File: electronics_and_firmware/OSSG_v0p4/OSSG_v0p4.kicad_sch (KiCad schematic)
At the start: 42 parts, among them J1 Conn_01x05_Male, Q1 2SC4617R BR, Q2 2SC4617R BR, SW1 SW_SPST, U1 SPH0645LMH, U2 ESP32-PICO-D4, U3 CH9102F

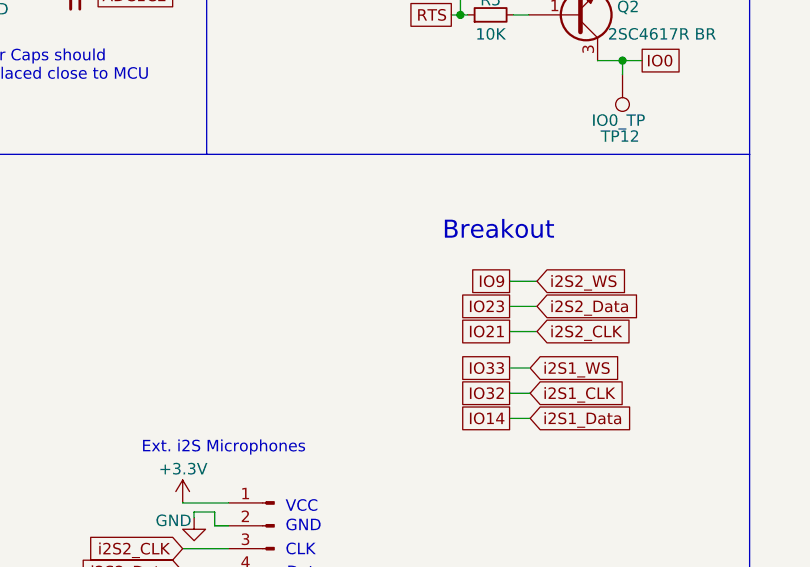
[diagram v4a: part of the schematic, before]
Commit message: adding in last update for the 2S branch design
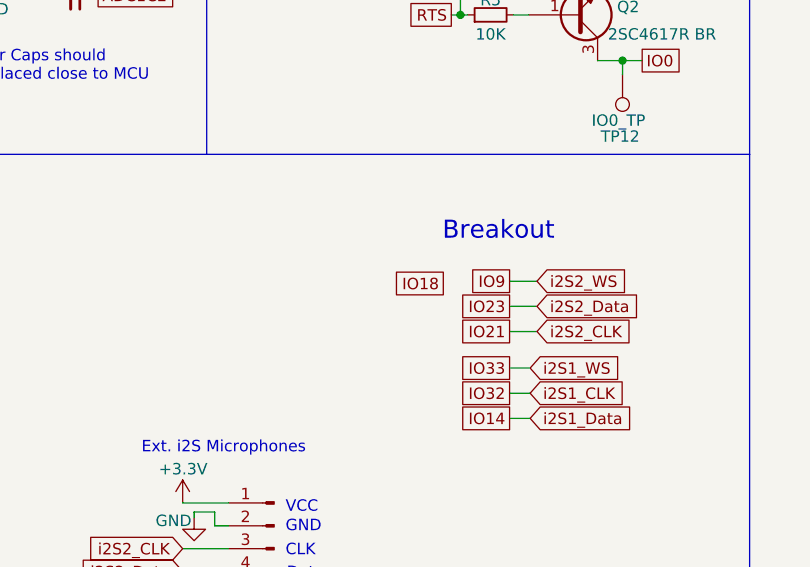
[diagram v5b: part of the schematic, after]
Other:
- title: Open Source Smart Glasses v0.4 -> Team OpenSource Smartglasses
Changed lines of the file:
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@@
   (paper "A3")
   (title_block
-    (title "Open Source Smart Glasses v0.4")
-    (date "2022-09-14")
-    (rev "0.4")
+    (title "Team OpenSource Smartglasses")
+    (date "2022-09-15")
+    (rev "V0.4b1")
     (company "Team Open Smart Glasses")
     (comment 1 "Design: Cayden Pierce, Nicholas Gray, Paul Hamilton")
@@
     (effects (font (size 1.27 1.27)) (justify right))
     (property "Intersheet References" "${INTERSHEET_REFS}" (id 0) (at 21.1726 82.4706 0)
+      (effects (font (size 1.27 1.27)) (justify right) hide)
+    )
+  )
+  (global_label "IO18" (shape passive) (at 143.002 227.076 180) (fields_autoplaced)
+    (effects (font (size 1.27 1.27)) (justify right))
+    (property "Intersheet References" "${INTERSHEET_REFS}" (id 0) (at 136.2346 227.1554 0)
       (effects (font (size 1.27 1.27)) (justify right) hide)
     )
@@
     )
     (path "/34a40e42-7107-4de0-9230-08b651254313/443ae60b-42e1-406e-9f4f-1af22a9043e4"
+      (reference "#PWR036") (unit 1) (value "GND") (footprint "")
+    )
+    (path "/34a40e42-7107-4de0-9230-08b651254313/a3325204-071c-4f8a-861c-930f69411704"
       (reference "#PWR037") (unit 1) (value "GND") (footprint "")
     )
-    (path "/34a40e42-7107-4de0-9230-08b651254313/a3325204-071c-4f8a-861c-930f69411704"
+    (path "/34a40e42-7107-4de0-9230-08b651254313/2eb7bef6-8281-41d6-9731-6d355fbc4c38"
       (reference "#PWR038") (unit 1) (value "GND") (footprint "")
     )
-    (path "/34a40e42-7107-4de0-9230-08b651254313/2eb7bef6-8281-41d6-9731-6d355fbc4c38"
+    (path "/34a40e42-7107-4de0-9230-08b651254313/7747ccd1-ec50-4486-bad1-0985e5a5163a"
       (reference "#PWR039") (unit 1) (value "GND") (footprint "")
     )
-    (path "/34a40e42-7107-4de0-9230-08b651254313/7747ccd1-ec50-4486-bad1-0985e5a5163a"
+    (path "/34a40e42-7107-4de0-9230-08b651254313/c809cdf9-07e3-480a-906d-7c50e11618c9"
       (reference "#PWR040") (unit 1) (value "GND") (footprint "")
     )
-    (path "/34a40e42-7107-4de0-9230-08b651254313/c809cdf9-07e3-480a-906d-7c50e11618c9"
+    (path "/34a40e42-7107-4de0-9230-08b651254313/b0de6b8f-d20d-4420-b55a-00724c30b12e"
       (reference "#PWR041") (unit 1) (value "GND") (footprint "")
     )
-    (path "/34a40e42-7107-4de0-9230-08b651254313/b0de6b8f-d20d-4420-b55a-00724c30b12e"
+    (path "/34a40e42-7107-4de0-9230-08b651254313/71c9eff5-7f20-4a02-9017-055904cec5a1"
       (reference "#PWR042") (unit 1) (value "GND") (footprint "")
     )
-    (path "/34a40e42-7107-4de0-9230-08b651254313/71c9eff5-7f20-4a02-9017-055904cec5a1"
-      (reference "#PWR043") (unit 1) (value "GND") (footprint "")
-    )
     (path "/34a40e42-7107-4de0-9230-08b651254313/4ed460d7-c332-4290-b5aa-89805711a2dc"
-      (reference "#PWR044") (unit 1) (value "+5V") (footprint "")
+      (reference "#PWR043") (unit 1) (value "+5V") (footprint "")
     )
     (path "/34a40e42-7107-4de0-9230-08b651254313/1a5aaa26-b096-4688-8357-02b3a0aa1142"
+      (reference "#PWR044") (unit 1) (value "GND") (footprint "")
+    )
+    (path "/34a40e42-7107-4de0-9230-08b651254313/1228ffe0-99b6-4bdc-b615-587a5f397285"
       (reference "#PWR045") (unit 1) (value "GND") (footprint "")
     )
-    (path "/34a40e42-7107-4de0-9230-08b651254313/1228ffe0-99b6-4bdc-b615-587a5f397285"
+    (path "/34a40e42-7107-4de0-9230-08b651254313/4deb7272-73c3-402e-a7d7-92cdf44f0279"
       (reference "#PWR046") (unit 1) (value "GND") (footprint "")
     )
-    (path "/34a40e42-7107-4de0-9230-08b651254313/4deb7272-73c3-402e-a7d7-92cdf44f0279"
+    (path "/34a40e42-7107-4de0-9230-08b651254313/c9f1220c-8a46-40f6-ac15-03b1135de33e"
       (reference "#PWR047") (unit 1) (value "GND") (footprint "")
     )
-    (path "/34a40e42-7107-4de0-9230-08b651254313/c9f1220c-8a46-40f6-ac15-03b1135de33e"
-      (reference "#PWR048") (unit 1) (value "GND") (footprint "")
-    )
     (path "/34a40e42-7107-4de0-9230-08b651254313/2994eed4-c7b8-474c-8407-807bee0af298"
-      (reference "#PWR049") (unit 1) (value "+3.3V") (footprint "")
+      (reference "#PWR048") (unit 1) (value "+3.3V") (footprint "")
     )
     (path "/777464b5-c722-47bf-99d3-1a7994e72d25"
@@
       (reference "R6") (unit 1) (value "100k") (footprint "Resistor_SMD:R_0402_1005Metric")
     )
+    (path "/34a40e42-7107-4de0-9230-08b651254313/ceade57a-c25e-4ab8-bf41-a92e98139556"
+      (reference "R7") (unit 1) (value "150") (footprint "Resistor_SMD:R_0402_1005Metric")
+    )
     (path "/34a40e42-7107-4de0-9230-08b651254313/ecae647e-071c-4f7a-96b1-e68d312fc410"
-      (reference "R7") (unit 1) (value "10K") (footprint "Resistor_SMD:R_0402_1005Metric")
+      (reference "R8") (unit 1) (value "10K") (footprint "Resistor_SMD:R_0402_1005Metric")
     )
     (path "/34a40e42-7107-4de0-9230-08b651254313/c0064630-51e3-4f04-a736-d6746cdfe5d1"
-      (reference "R8") (unit 1) (value "2K") (footprint "Resistor_SMD:R_0402_1005Metric")
+      (reference "R9") (unit 1) (value "2K") (footprint "Resistor_SMD:R_0402_1005Metric")
     )
     (path "/34a40e42-7107-4de0-9230-08b651254313/727c3385-0c0e-43bc-85be-dbf17c658b39"
-      (reference "R9") (unit 1) (value "2K") (footprint "Resistor_SMD:R_0402_1005Metric")
+      (reference "R10") (unit 1) (value "2K") (footprint "Resistor_SMD:R_0402_1005Metric")
     )
     (path "/34a40e42-7107-4de0-9230-08b651254313/79808270-03c5-470d-b78a-cf5c807253d4"
-      (reference "R10") (unit 1) (value "100K") (footprint "Resistor_SMD:R_0402_1005Metric")
+      (reference "R11") (unit 1) (value "100K") (footprint "Resistor_SMD:R_0402_1005Metric")
     )
     (path "/34a40e42-7107-4de0-9230-08b651254313/30942408-6643-491f-be92-1d34808610d1"
-      (reference "R15") (unit 1) (value "884K") (footprint "Resistor_SMD:R_0402_1005Metric")
+      (reference "R12") (unit 1) (value "884K") (footprint "Resistor_SMD:R_0402_1005Metric")
     )
     (path "/34a40e42-7107-4de0-9230-08b651254313/fa8472fd-240f-469e-ab98-9afe4434bfe3"
-      (reference "R16") (unit 1) (value "320K") (footprint "Resistor_SMD:R_0402_1005Metric")
+      (reference "R13") (unit 1) (value "320K") (footprint "Resistor_SMD:R_0402_1005Metric")
     )
     (path "/34a40e42-7107-4de0-9230-08b651254313/b33a0bfd-f29a-42b9-850c-92d0d06ecdb9"
-      (reference "R17") (unit 1) (value ".025") (footprint "Resistor_SMD:R_0402_1005Metric")
+      (reference "R14") (unit 1) (value ".025") (footprint "Resistor_SMD:R_0402_1005Metric")
     )
     (path "/34a40e42-7107-4de0-9230-08b651254313/0c5a8c0d-eec1-4f56-ba60-65c26e14e5d7"
-      (reference "R18") (unit 1) (value "100K") (footprint "Resistor_SMD:R_0402_1005Metric")
+      (reference "R15") (unit 1) (value "100K") (footprint "Resistor_SMD:R_0402_1005Metric")
     )
     (path "/34a40e42-7107-4de0-9230-08b651254313/d717a7ff-d559-47bb-a771-b48dc3597435"
-      (reference "R19") (unit 1) (value "884K") (footprint "Resistor_SMD:R_0402_1005Metric")
+      (reference "R16") (unit 1) (value "884K") (footprint "Resistor_SMD:R_0402_1005Metric")
     )
     (path "/34a40e42-7107-4de0-9230-08b651254313/a326c3cb-19ca-490f-9d5f-7bba433eb65f"
-      (reference "R20") (unit 1) (value "100K") (footprint "Resistor_SMD:R_0402_1005Metric")
+      (reference "R17") (unit 1) (value "100K") (footprint "Resistor_SMD:R_0402_1005Metric")
     )
     (path "/92534179-acae-4912-baf5-95c7fd0a3d18"
